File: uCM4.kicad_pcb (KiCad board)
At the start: 2 copper layers, 55 x 48 mm, 77 parts, among them IC1 MAX17048G+, J10 USB_C_Receptacle, J11 SolderJumper_2_Open, J12 Conn_02x08_Odd_Even, J13 Conn_02x07_Odd_Even, J2 Micro_SD_Card_Det, J4 Conn_01x04, J5 DummyJ, J6 DummyJ, J7 SolderJumper_2_Open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

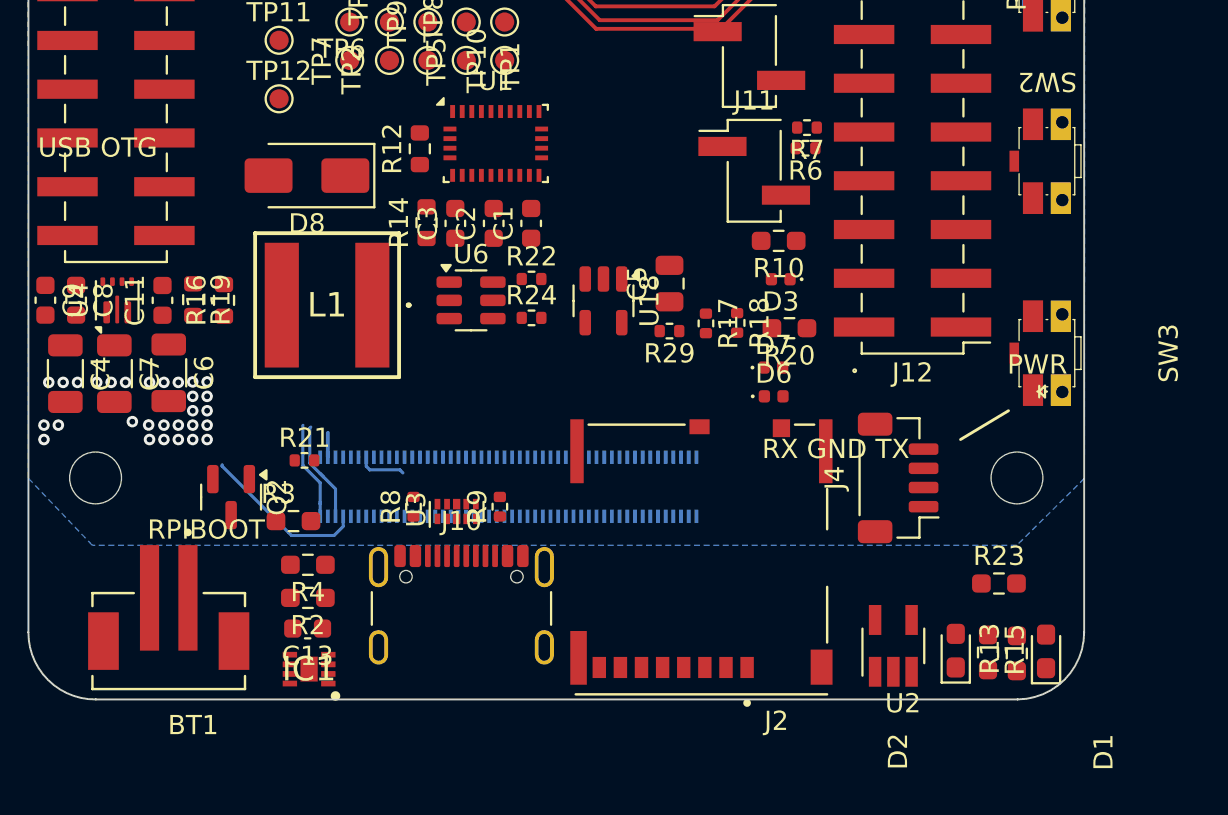
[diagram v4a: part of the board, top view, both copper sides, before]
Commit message: Updated USB-C connector to be simpler.
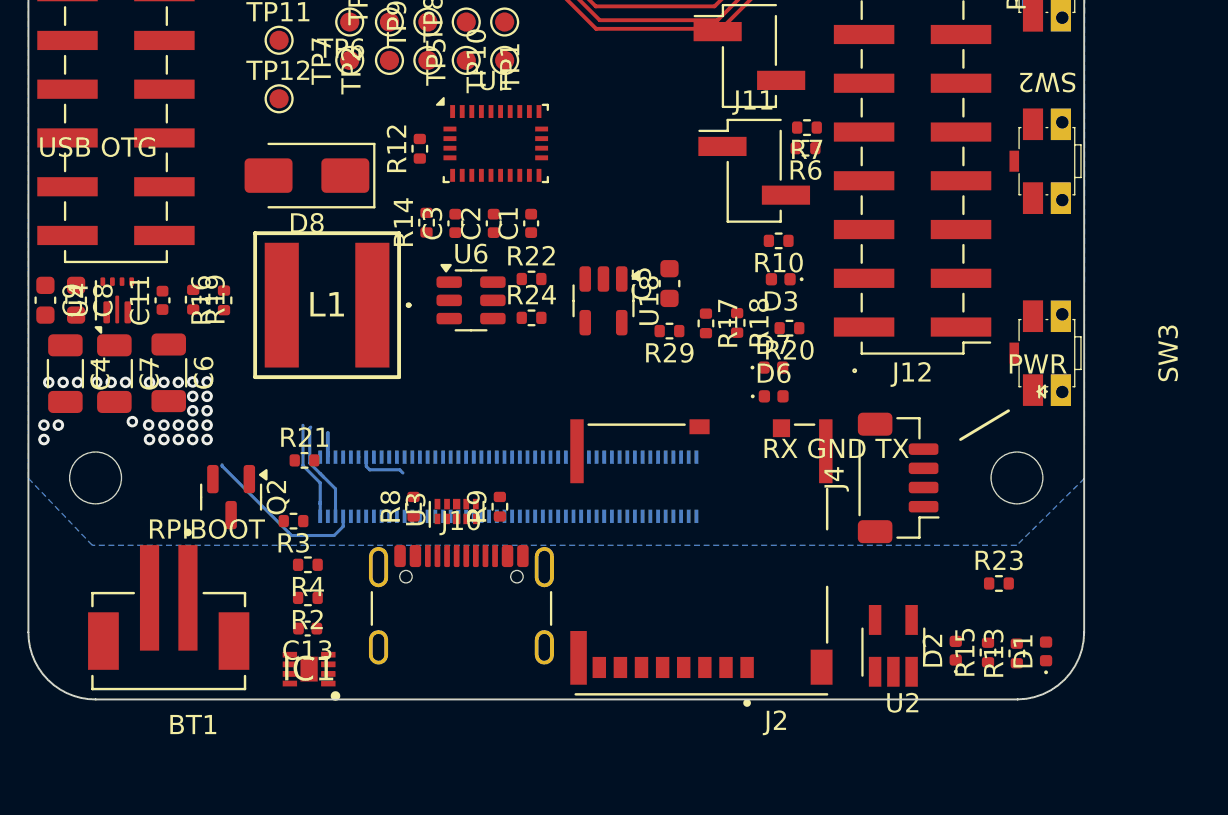
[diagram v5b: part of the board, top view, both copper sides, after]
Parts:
- C1, C11, C13, C2, C3: footprint Capacitor_SMD:C_0603_1608Metric -> Capacitor_SMD:C_0402_1005Metric
- C5: footprint Capacitor_SMD:C_0805_2012Metric -> Capacitor_SMD:C_0603_1608Metric
- D1, D2: footprint LED_SMD:LED_0603_1608Metric_Pad1.05x0.95mm_HandSolder -> LED_SMD:LED_0402_1005Metric
- R10, R13, R15, R2, R20, R23, R3, R4: footprint Resistor_SMD:R_0603_1608Metric_Pad0.98x0.95mm_HandSolder -> Resistor_SMD:R_0402_1005Metric
- R12, R14, R16, R19: footprint Resistor_SMD:R_0603_1608Metric -> Resistor_SMD:R_0402_1005Metric
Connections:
- J10 pad A8: unconnected-(J10-SBU1-PadA8) -> (no net)
- J10 pad B8: unconnected-(J10-SBU2-PadB8) -> (no net)

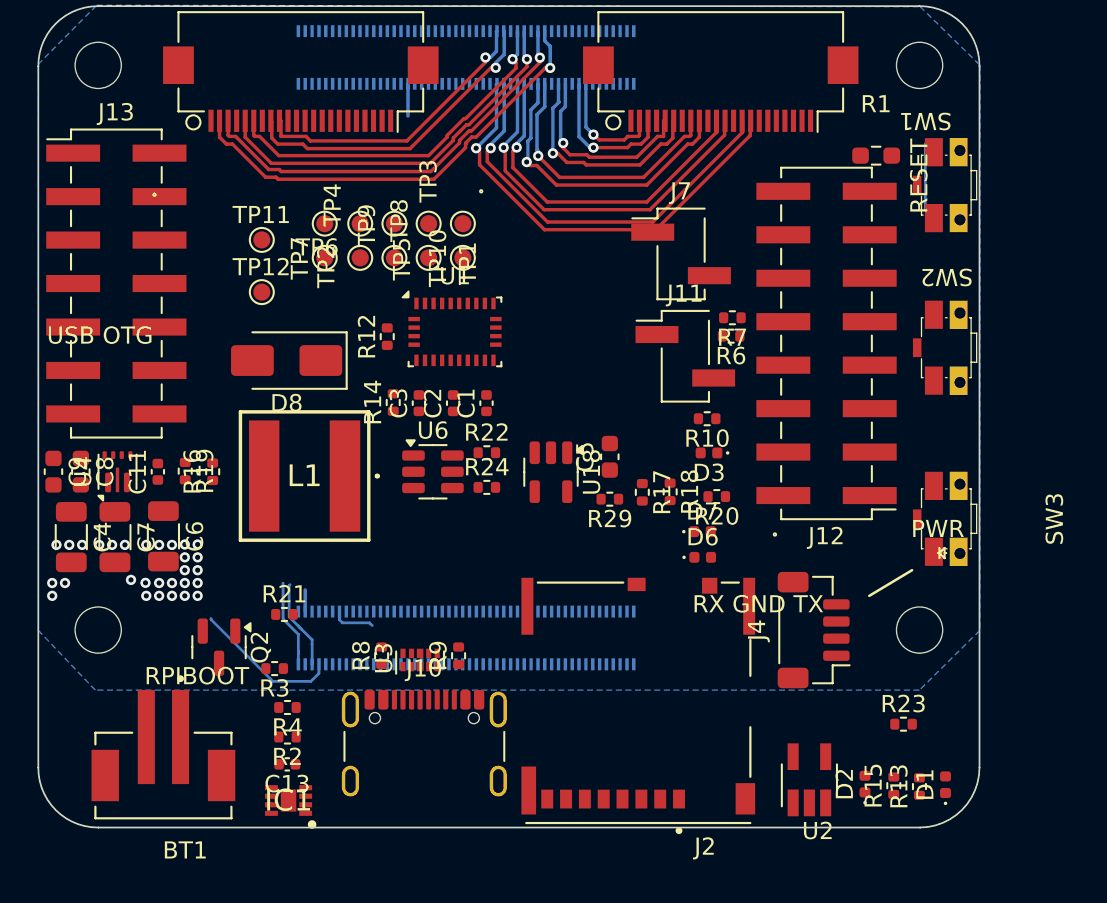
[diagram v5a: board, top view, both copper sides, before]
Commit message: Arranging and changing switches.
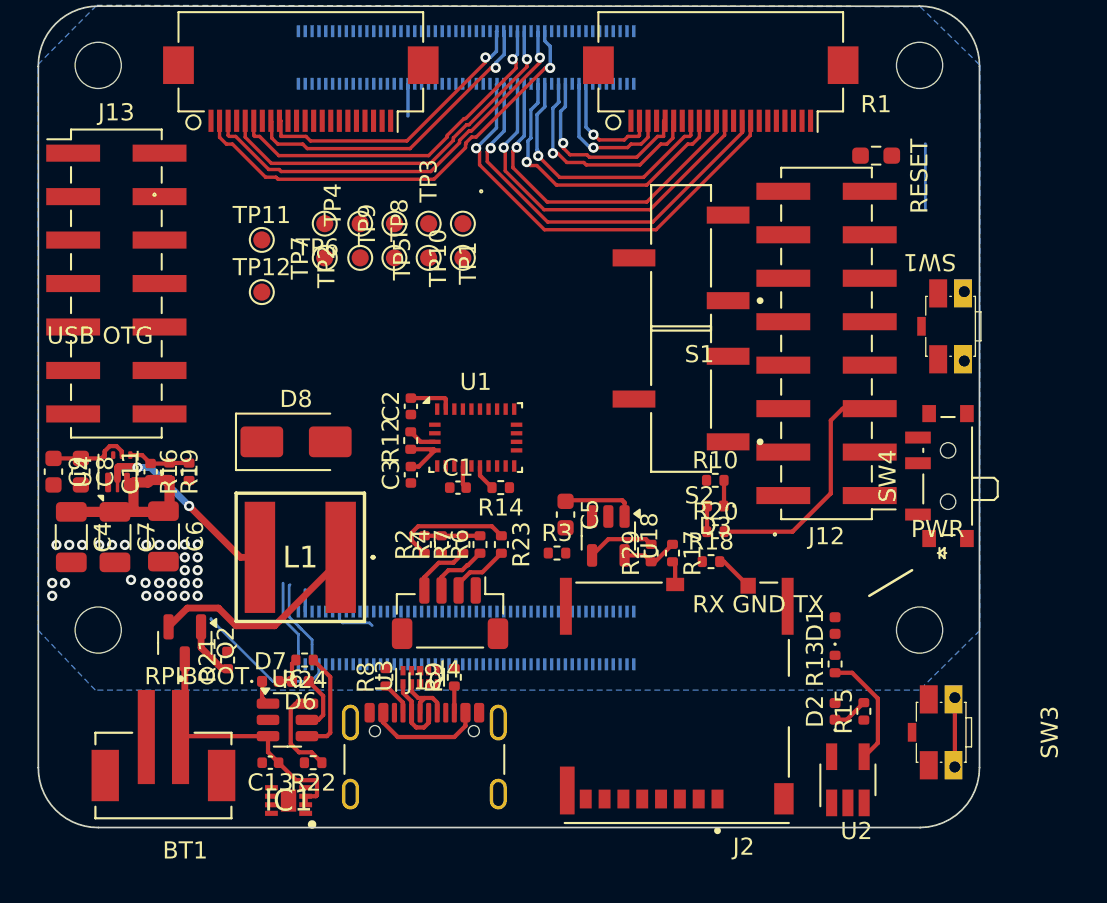
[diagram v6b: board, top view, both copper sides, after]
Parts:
- removed J11, J7: SolderJumper_2_Open, Connector_PinHeader_2.54mm:PinHeader_1x02_P2.54mm_Vertical_SMD_Pin1Left
- removed SW2: SW_DIP_x01, KiCAD_Randoms:PTS840_PM_SMTR_LFS
- added S1: JS102011SCQN, CM4:SW_JS102011SCQN, F.Cu at (158.5, 99.8)
- added S2: JS102011SCQN, CM4:SW_JS102011SCQN, F.Cu at (158.5, 108.0)
- added SW4: SW_SPDT, Button_Switch_SMD:SW_SPDT_PCM12, F.Cu at (173.8, 112.5)
- moved D7 26.7 mm to (134.5, 124.5)
- moved R23 25.7 mm to (148.0, 116.5), turned to -90 degrees
- moved D6 24.6 mm to (136.2, 124.5), turned to 180 degrees
- moved J4 21.3 mm to (145.0, 120.5), turned to 180 degrees
- moved R22 20.8 mm to (137.0, 129.2), turned to 180 degrees
- moved R7 20.6 mm to (145.8, 116.5), turned to 90 degrees
- moved R6 19.1 mm to (146.8, 116.5), turned to 90 degrees
- moved R3 17.8 mm to (151.2, 117.0), turned to 0 degrees
- moved U6 16.8 mm to (135.5, 126.8)
- moved R24 14.7 mm to (136.5, 123.2), turned to 180 degrees
- moved R2 13.8 mm to (143.5, 116.5), turned to 90 degrees
- moved R4 13.1 mm to (144.5, 116.5), turned to 90 degrees
- moved SW3 12.5 mm to (173.7, 127.5)
- moved D1 11.3 mm to (167.5, 121.2)
- moved R13 8.69 mm to (167.5, 123.5)
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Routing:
- net /BOOST_IN: track 0.00 -> 17.5 mm
- net /BAT: track 0.00 -> 16.3 mm
- net VBUS: track 0.00 -> 16.1 mm
- net +3V3: track 0.00 -> 14.5 mm
- net Net-(J12-Pin_5): track 0.00 -> 14.0 mm
- net Net-(U4-SW): track 0.00 -> 11.3 mm, vias 0 -> 2
- net +5V: track 0.00 -> 11.2 mm
- net /nPWR_LED_Buffered: track 0.00 -> 6.85 mm
- net Net-(U6-PROG): track 0.00 -> 5.41 mm
- net /SD_PWR: track 0.00 -> 4.34 mm
- net /USB_N: track 0.00 -> 4.29 mm
- net /BTN0: track 0.00 -> 4.05 mm
- net /SD_PWR_ON: track 0.00 -> 3.97 mm
- net /USB_P: track 0.00 -> 3.77 mm
- net Net-(U4-FB): track 0.00 -> 3.65 mm
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
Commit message: Routing
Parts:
- moved U3 7.28 mm to (150.2, 126.2), turned to 0 degrees
- moved R9 0.70 mm to (145.8, 124.8), turned to 0 degrees
- moved R8 0.50 mm to (140.8, 124.2)
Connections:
- U3 pad 2: /USB_P -> unconnected-(U3-D1--Pad2)
- U3 pad 5: unconnected-(U3-D2--Pad5) -> /USB_P
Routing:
- net /SDA0: track 0.00 -> 45.2 mm, vias 0 -> 4
- net /CTS0: track 0.00 -> 40.5 mm, vias 0 -> 1
- net /SCL0: track 0.00 -> 40.2 mm, vias 0 -> 4
- net /RXD3: track 0.00 -> 37.5 mm, vias 0 -> 1
- net /GPS_TIME_1: track 0.00 -> 37.4 mm, vias 0 -> 1
- net /RXD4: track 0.00 -> 36.5 mm, vias 0 -> 3
- net /SPI6_MOSI: track 0.00 -> 35.6 mm, vias 0 -> 1
- net /TXD4: track 0.00 -> 35.5 mm, vias 0 -> 3
- net /GPS_READY: track 0.00 -> 33.8 mm, vias 0 -> 1
- net /SPI6_SCLK: track 0.00 -> 33.8 mm, vias 0 -> 1
- net /TXD3: track 0.00 -> 33.1 mm, vias 0 -> 1
- net /SPI6_MISO: track 0.00 -> 32.6 mm, vias 0 -> 1
- net /GPS_TIME_2: track 0.00 -> 31.1 mm, vias 0 -> 1
- net VBUS: track 16.1 -> 43.9 mm, vias 0 -> 2
- net /SD_PWR: track 4.34 -> 28.1 mm
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
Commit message: Correcting symbols and routing progress.
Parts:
- D1, D2, D3, D6, D7, R10, R13, R15, R24: moved to B.Cu
- moved R10 19.0 mm to (157.3, 131.4)
- moved D3 16.0 mm to (157.3, 129.9)
- moved R24 10.8 mm to (128.4, 130.4), turned to 0 degrees
- moved D6 10.4 mm to (128.6, 131.6), turned to 0 degrees
- moved D1 9.94 mm to (167.2, 131.2), turned to 180 degrees
- moved D7 8.23 mm to (130.4, 131.6), turned to 180 degrees
- moved R15 8.18 mm to (162.7, 131.2)
- moved R13 7.95 mm to (169.5, 131.2), turned to 180 degrees
- moved D2 5.87 mm to (164.3, 131.2)
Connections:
- BT1 pad S1: (no net) -> GND
- BT1 pad S2: (no net) -> GND
- J10 pad A8: (no net) -> unconnected-(J10-SBU1-PadA8)
- J10 pad B8: (no net) -> unconnected-(J10-SBU1-PadB8)
- J4 pad MP: (no net) -> GND
- J8 pad MP: (no net) -> GND
- J9 pad MP: (no net) -> GND
- U2 pad 1: (no net) -> unconnected-(U2-NC-Pad1)
